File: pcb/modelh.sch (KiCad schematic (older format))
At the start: 43 parts, among them J1 USB_B, J2 Conn_01x16, J3 Conn_01x12, J4 Conn_01x04, J5 Conn_02x03_Odd_Even, J6 Conn_02x05_Odd_Even, SW1 SW_Push, U1 STM32F103C8Tx, U2 AMS1117-3.3, Y1 8MHz, Y2 32.768KHz

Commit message: WIP
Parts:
- removed D1: B5819W, Diode_SMD:D_SOD-123, symbol Device:D_Schottky
- added R?: 0, symbol Device:R
- R7, R8, R9: value 120 -> 60; footprint Resistor_SMD:R_0603_1608Metric -> Resistor_SMD:R_0805_2012Metric
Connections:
- net +5V: now also R?.1
- net D+: now also R11.1
- net D-: no longer R11.1
- net at J1.1 (VBUS): now also R?.2
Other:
- moved on the sheet: R11
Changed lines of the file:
@@
 P 8900 4600
 F 0 "R7" V 8850 4750 50  0000 C CNN
-F 1 "120" V 8900 4600 50  0000 C CNN
-F 2 "Resistor_SMD:R_0603_1608Metric" V 8830 4600 50  0001 C CNN
+F 1 "60" V 8900 4600 50  0000 C CNN
+F 2 "Resistor_SMD:R_0805_2012Metric" V 8830 4600 50  0001 C CNN
 F 3 "~" H 8900 4600 50  0001 C CNN
 F 4 "C22787" H 8900 4600 50  0001 C CNN "LCSC"
@@
 P 8900 4700
 F 0 "R8" V 8850 4850 50  0000 C CNN
-F 1 "120" V 8900 4700 50  0000 C CNN
-F 2 "Resistor_SMD:R_0603_1608Metric" V 8830 4700 50  0001 C CNN
+F 1 "60" V 8900 4700 50  0000 C CNN
+F 2 "Resistor_SMD:R_0805_2012Metric" V 8830 4700 50  0001 C CNN
 F 3 "~" H 8900 4700 50  0001 C CNN
 F 4 "C22787" H 8900 4700 50  0001 C CNN "LCSC"
@@
 P 8900 4900
 F 0 "R9" V 8850 5050 50  0000 C CNN
-F 1 "120" V 8900 4900 50  0000 C CNN
-F 2 "Resistor_SMD:R_0603_1608Metric" V 8830 4900 50  0001 C CNN
+F 1 "60" V 8900 4900 50  0000 C CNN
+F 2 "Resistor_SMD:R_0805_2012Metric" V 8830 4900 50  0001 C CNN
 F 3 "~" H 8900 4900 50  0001 C CNN
 F 4 "C22787" H 8900 4900 50  0001 C CNN "LCSC"
@@
 L power:+5V #PWR0104
 U 1 1 5EDAFF6A
-P 2250 1000
-F 0 "#PWR0104" H 2250 850 50  0001 C CNN
-F 1 "+5V" H 2265 1173 50  0000 C CNN
-F 2 "" H 2250 1000 50  0001 C CNN
-F 3 "" H 2250 1000 50  0001 C CNN
-	1    2250 1000
+P 2150 900
+F 0 "#PWR0104" H 2150 750 50  0001 C CNN
+F 1 "+5V" H 2165 1073 50  0000 C CNN
+F 2 "" H 2150 900 50  0001 C CNN
+F 3 "" H 2150 900 50  0001 C CNN
+	1    2150 900
 	1    0    0    -1
 $EndComp
 Wire Wire Line
 	1700 1100 1800 1100
-Wire Wire Line
-	2250 1100 2250 1000
 $Comp
 L Device:R R3
@@
 Wire Wire Line
 	1700 1400 1800 1400
-Wire Wire Line
-	2100 1400 2200 1400
 $Comp
 L Device:C C5
@@
 L Device:R R11
 U 1 1 5F3ACB58
-P 2200 1550
-F 0 "R11" H 2270 1596 50  0000 L CNN
-F 1 "1.5k" H 2270 1505 50  0000 L CNN
-F 2 "Resistor_SMD:R_0603_1608Metric" V 2130 1550 50  0001 C CNN
-F 3 "~" H 2200 1550 50  0001 C CNN
-	1    2200 1550
-	1    0    0    -1
-$EndComp
-Wire Wire Line
-	2350 1400 2200 1400
-Connection ~ 2200 1400
-Wire Wire Line
-	2100 1300 2350 1300
+P 2400 1100
+F 0 "R11" H 2470 1146 50  0000 L CNN
+F 1 "1.5k" H 2470 1055 50  0000 L CNN
+F 2 "Resistor_SMD:R_0603_1608Metric" V 2330 1100 50  0001 C CNN
+F 3 "~" H 2400 1100 50  0001 C CNN
+	1    2400 1100
+	-1   0    0    1
+$EndComp
 $Comp
 L power:+5V #PWR0124
 U 1 1 5F3CEBAA
-P 2200 1700
-F 0 "#PWR0124" H 2200 1550 50  0001 C CNN
-F 1 "+5V" H 2215 1873 50  0000 C CNN
-F 2 "" H 2200 1700 50  0001 C CNN
-F 3 "" H 2200 1700 50  0001 C CNN
-	1    2200 1700
-	-1   0    0    1
-$EndComp
-$Comp
-L Device:D_Schottky D1
-U 1 1 5F3E67EF
-P 1950 1100
-F 0 "D1" H 1950 884 50  0000 C CNN
-F 1 "B5819W" H 1950 975 50  0000 C CNN
-F 2 "Diode_SMD:D_SOD-123" H 1950 1100 50  0001 C CNN
-F 3 "~" H 1950 1100 50  0001 C CNN
-	1    1950 1100
-	-1   0    0    1
-$EndComp
-Wire Wire Line
-	2100 1100 2250 1100
+P 2400 950
+F 0 "#PWR0124" H 2400 800 50  0001 C CNN
+F 1 "+5V" H 2415 1123 50  0000 C CNN
+F 2 "" H 2400 950 50  0001 C CNN
+F 3 "" H 2400 950 50  0001 C CNN
+	1    2400 950
+	1    0    0    -1
+$EndComp
 Wire Wire Line
 	2900 5150 3200 5150
@@
 Text GLabel 8450 4900 0    50   Input ~ 0
 led2
-Text GLabel 2350 1300 2    50   Input ~ 0
+Text GLabel 2550 1300 2    50   Input ~ 0
 D+
-Text GLabel 2350 1400 2    50   Input ~ 0
+Text GLabel 2550 1400 2    50   Input ~ 0
 D-
 Text GLabel 1250 5150 0    50   Input ~ 0
@@
 Wire Wire Line
 	10100 4000 9900 4000
+Wire Wire Line
+	2400 1300 2400 1250
+Wire Wire Line
+	2100 1100 2150 1100
+Wire Wire Line
+	2150 1100 2150 900
+Wire Wire Line
+	2400 1300 2100 1300
+Wire Wire Line
+	2550 1300 2400 1300
+Connection ~ 2400 1300
+Wire Wire Line
+	2550 1400 2100 1400
+$Comp
+L Device:R R?
+U 1 1 5F9EF12F
+P 1950 1100
+F 0 "R?" V 1743 1100 50  0000 C CNN
+F 1 "0" V 1834 1100 50  0000 C CNN
+F 2 "" V 1880 1100 50  0001 C CNN
+F 3 "~" H 1950 1100 50  0001 C CNN
+	1    1950 1100
+	0    1    1    0
+$EndComp
 $EndSCHEMATC

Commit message: WIP
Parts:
- R16: renamed from R?; footprint (none) -> Resistor_SMD:R_0805_2012Metric_Pad1.15x1.40mm_HandSolder
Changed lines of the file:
@@
 	2550 1400 2100 1400
 $Comp
-L Device:R R?
+L Device:R R16
 U 1 1 5F9EF12F
 P 1950 1100
-F 0 "R?" V 1743 1100 50  0000 C CNN
+F 0 "R16" V 1743 1100 50  0000 C CNN
 F 1 "0" V 1834 1100 50  0000 C CNN
-F 2 "" V 1880 1100 50  0001 C CNN
+F 2 "Resistor_SMD:R_0805_2012Metric_Pad1.15x1.40mm_HandSolder" V 1880 1100 50  0001 C CNN
 F 3 "~" H 1950 1100 50  0001 C CNN
 	1    1950 1100

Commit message: WIP
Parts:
- J2: footprint Connector_PinHeader_2.54mm:PinHeader_1x16_P2.54mm_Vertical -> Connector_PinSocket_2.54mm:PinSocket_1x16_P2.54mm_Vertical
- J4: footprint Connector_PinHeader_2.54mm:PinHeader_1x04_P2.54mm_Vertical -> Connector_PinSocket_2.54mm:PinSocket_1x04_P2.54mm_Vertical
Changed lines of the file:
@@
 F 0 "J2" H 10380 1942 50  0000 L CNN
 F 1 "Conn_01x16" H 10380 1851 50  0000 L CNN
-F 2 "Connector_PinHeader_2.54mm:PinHeader_1x16_P2.54mm_Vertical" H 10300 1950 50  0001 C CNN
+F 2 "Connector_PinSocket_2.54mm:PinSocket_1x16_P2.54mm_Vertical" H 10300 1950 50  0001 C CNN
 F 3 "~" H 10300 1950 50  0001 C CNN
 	1    10300 1950
@@
 F 0 "J4" H 10380 4692 50  0000 L CNN
 F 1 "Conn_01x04" H 10380 4601 50  0000 L CNN
-F 2 "Connector_PinHeader_2.54mm:PinHeader_1x04_P2.54mm_Vertical" H 10300 4700 50  0001 C CNN
+F 2 "Connector_PinSocket_2.54mm:PinSocket_1x04_P2.54mm_Vertical" H 10300 4700 50  0001 C CNN
 F 3 "~" H 10300 4700 50  0001 C CNN
 	1    10300 4700

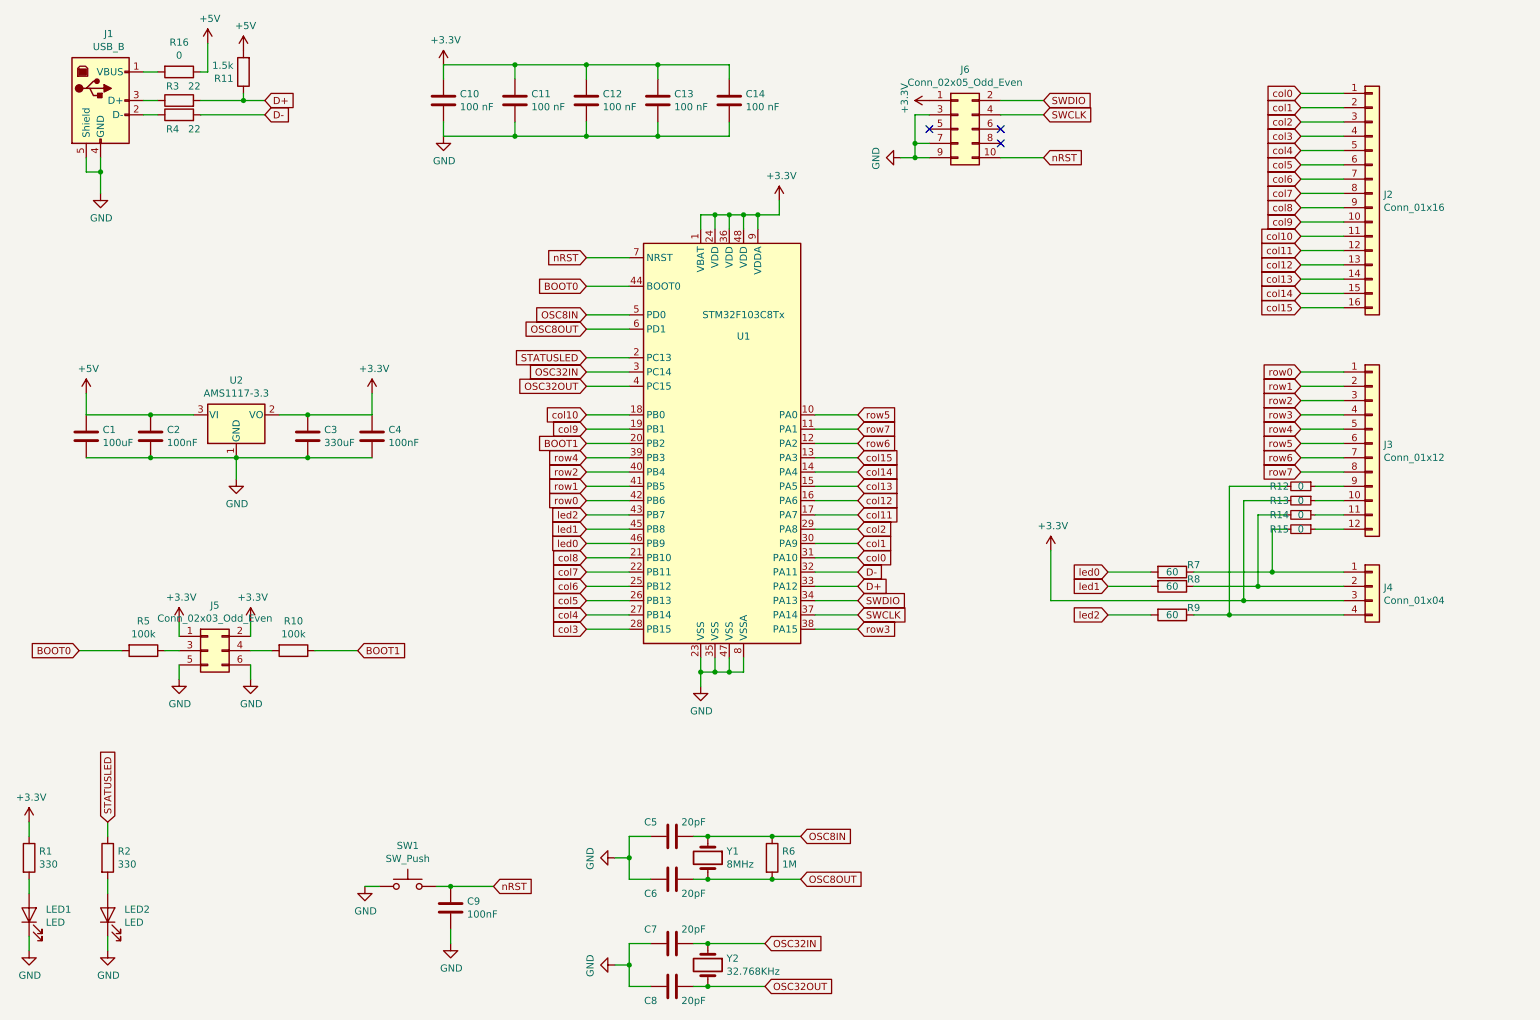
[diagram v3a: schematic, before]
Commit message: Remove LSE oscillator
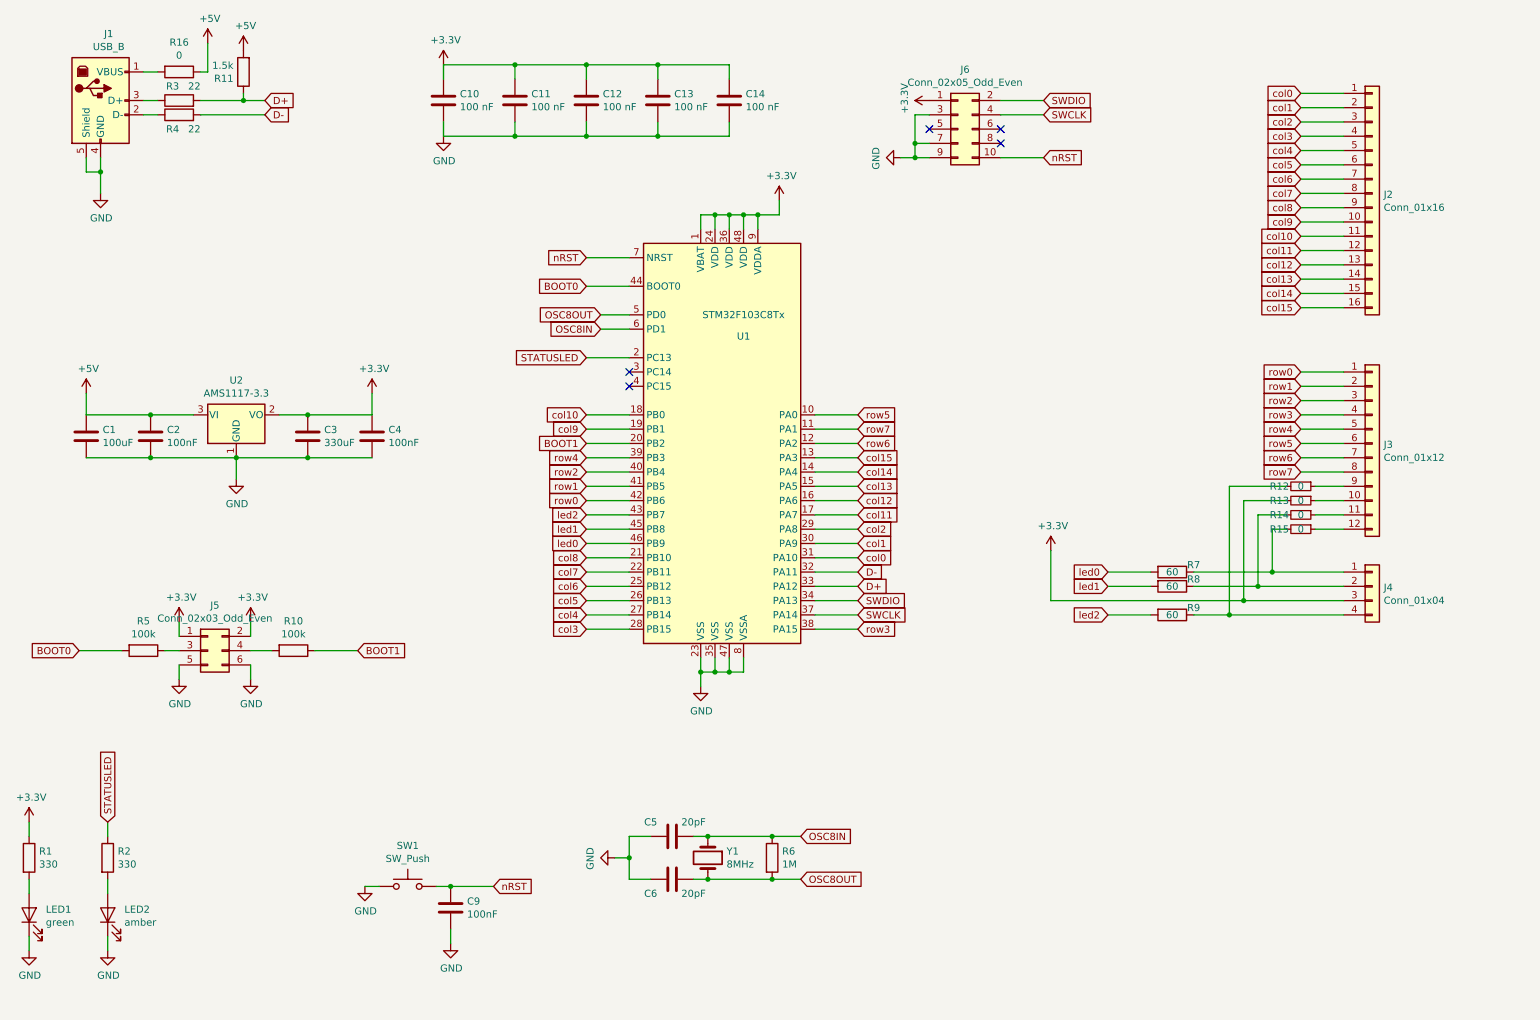
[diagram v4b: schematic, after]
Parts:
- removed C7, C8: 20pF, Capacitor_SMD:C_0603_1608Metric, symbol Device:C
- removed Y2: 32.768KHz, Crystal:Crystal_SMD_3215-2Pin_3.2x1.5mm, symbol Device:Crystal
- LED1: value LED -> green
- LED2: value LED -> amber
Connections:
- net OSC8IN: now also U1.6 (PD1); no longer U1.5 (PD0)
- net OSC8OUT: now also U1.5 (PD0); no longer U1.6 (PD1)
- net OSC32IN: no longer names the net of U1.3 (PC14)
- net OSC32OUT: no longer names the net of U1.4 (PC15)
- no-connect marks 3 -> 5
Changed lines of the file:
@@
 P 900 7000
 F 0 "LED1" V 939 6883 50  0000 R CNN
-F 1 "LED" V 848 6883 50  0000 R CNN
+F 1 "green" V 848 6883 50  0000 R CNN
 F 2 "LED_SMD:LED_0805_2012Metric" H 900 7000 50  0001 C CNN
 F 3 "~" H 900 7000 50  0001 C CNN
@@
 	5100 4100 4800 4100
 Wire Wire Line
-	5100 2800 4800 2800
-Wire Wire Line
-	4800 2900 5100 2900
-Wire Wire Line
-	5100 3200 4800 3200
-Wire Wire Line
-	4800 3300 5100 3300
-Wire Wire Line
 	5100 2400 4800 2400
 Wire Wire Line
@@
 Wire Wire Line
 	5550 6750 5650 6750
-$Comp
-L Device:C C7
-U 1 1 5F13915E
-P 5400 7200
-F 0 "C7" V 5300 7050 50  0000 C CNN
-F 1 "20pF" V 5300 7350 50  0000 C CNN
-F 2 "Capacitor_SMD:C_0603_1608Metric" H 5438 7050 50  0001 C CNN
-F 3 "~" H 5400 7200 50  0001 C CNN
-F 4 "C1653" H 5400 7200 50  0001 C CNN "LCSC"
-	1    5400 7200
-	0    1    1    0
-$EndComp
-$Comp
-L Device:C C8
-U 1 1 5F139165
-P 5400 7500
-F 0 "C8" V 5500 7350 50  0000 C CNN
-F 1 "20pF" V 5500 7650 50  0000 C CNN
-F 2 "Capacitor_SMD:C_0603_1608Metric" H 5438 7350 50  0001 C CNN
-F 3 "~" H 5400 7500 50  0001 C CNN
-F 4 "C1653" H 5400 7500 50  0001 C CNN "LCSC"
-	1    5400 7500
-	0    1    1    0
-$EndComp
-Wire Wire Line
-	5250 7200 5100 7200
-Wire Wire Line
-	5100 7500 5250 7500
-Wire Wire Line
-	5100 7200 5100 7350
-$Comp
-L power:GND #PWR0106
-U 1 1 5F13916E
-P 5000 7350
-F 0 "#PWR0106" H 5000 7100 50  0001 C CNN
-F 1 "GND" H 5005 7177 50  0000 C CNN
-F 2 "" H 5000 7350 50  0001 C CNN
-F 3 "" H 5000 7350 50  0001 C CNN
-	1    5000 7350
-	0    1    1    0
-$EndComp
-Connection ~ 5100 7350
-Wire Wire Line
-	5100 7350 5100 7500
-Wire Wire Line
-	5000 7350 5100 7350
-$Comp
-L Device:Crystal Y2
-U 1 1 5F139177
-P 5650 7350
-F 0 "Y2" V 5604 7481 50  0000 L CNN
-F 1 "32.768KHz" V 5695 7481 50  0000 L CNN
-F 2 "Crystal:Crystal_SMD_3215-2Pin_3.2x1.5mm" H 5650 7350 50  0001 C CNN
-F 3 "~" H 5650 7350 50  0001 C CNN
-	1    5650 7350
-	0    1    1    0
-$EndComp
-Wire Wire Line
-	5550 7200 5650 7200
-Connection ~ 5650 7200
-Wire Wire Line
-	5550 7500 5650 7500
-Connection ~ 5650 7500
 $Comp
 L Device:R R6
@@
 Connection ~ 5650 6750
 Wire Wire Line
-	5650 7200 6050 7200
-Wire Wire Line
-	5650 7500 6050 7500
-Wire Wire Line
 	6300 6750 6100 6750
 Connection ~ 6100 6750
@@
 P 1450 7000
 F 0 "LED2" V 1489 6883 50  0000 R CNN
-F 1 "LED" V 1398 6883 50  0000 R CNN
+F 1 "amber" V 1398 6883 50  0000 R CNN
 F 2 "LED_SMD:LED_0805_2012Metric" H 1450 7000 50  0001 C CNN
 F 3 "~" H 1450 7000 50  0001 C CNN
@@
 Text GLabel 4150 6800 2    50   Input ~ 0
 nRST
-Text GLabel 6050 7500 2    50   Input ~ 0
-OSC32OUT
-Text GLabel 6050 7200 2    50   Input ~ 0
-OSC32IN
 Text GLabel 6300 6750 2    50   Input ~ 0
 OSC8OUT
@@
 Text GLabel 4800 2600 0    50   Input ~ 0
 BOOT0
-Text GLabel 4800 2800 0    50   Input ~ 0
-OSC8IN
-Text GLabel 4800 2900 0    50   Input ~ 0
-OSC8OUT
 Text GLabel 4800 3100 0    50   Input ~ 0
 STATUSLED
-Text GLabel 4800 3200 0    50   Input ~ 0
-OSC32IN
-Text GLabel 4800 3300 0    50   Input ~ 0
-OSC32OUT
 Text GLabel 4800 3500 0    50   Input ~ 0
 col10
@@
 	0    1    1    0
 $EndComp
+Wire Wire Line
+	4900 2800 5100 2800
+Wire Wire Line
+	4900 2900 5100 2900
+Text GLabel 4900 2800 0    50   Input ~ 0
+OSC8OUT
+Text GLabel 4900 2900 0    50   Input ~ 0
+OSC8IN
+NoConn ~ 5100 3200
+NoConn ~ 5100 3300
 $EndSCHEMATC

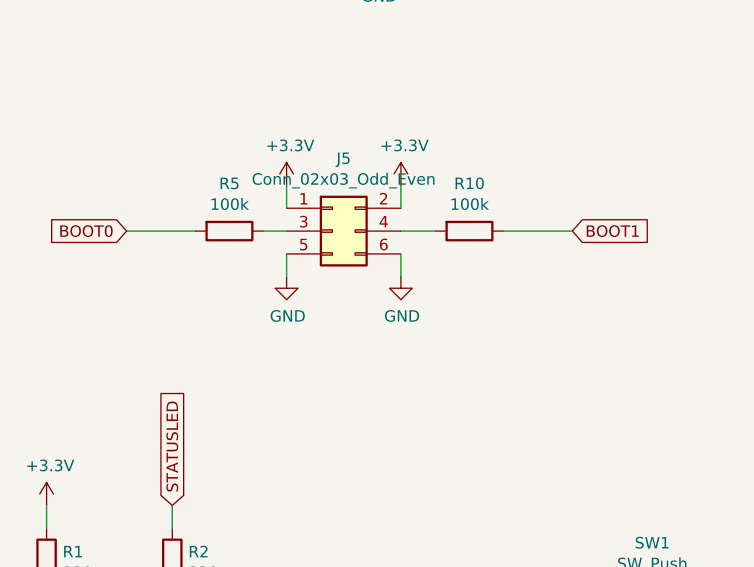
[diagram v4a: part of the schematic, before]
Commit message: Make boot selection pins optional
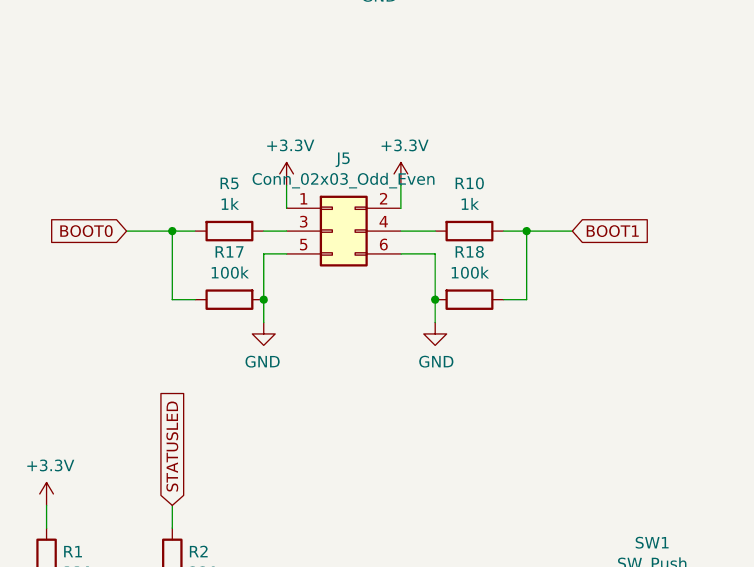
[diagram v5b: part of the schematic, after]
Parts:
- added R17, R18: 100k, Resistor_SMD:R_0603_1608Metric, symbol Device:R
- R10, R5: value 100k -> 1k
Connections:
- net BOOT0: now also R17.1
- net BOOT1: now also R18.1
- net GND: now also R17.2, R18.2
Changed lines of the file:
@@
 P 2750 5150
 F 0 "R10" V 2543 5150 50  0000 C CNN
-F 1 "100k" V 2634 5150 50  0000 C CNN
+F 1 "1k" V 2634 5150 50  0000 C CNN
 F 2 "Resistor_SMD:R_0603_1608Metric" V 2680 5150 50  0001 C CNN
 F 3 "~" H 2750 5150 50  0001 C CNN
@@
 P 1700 5150
 F 0 "R5" V 1493 5150 50  0000 C CNN
-F 1 "100k" V 1584 5150 50  0000 C CNN
+F 1 "1k" V 1584 5150 50  0000 C CNN
 F 2 "Resistor_SMD:R_0603_1608Metric" V 1630 5150 50  0001 C CNN
 F 3 "~" H 1700 5150 50  0001 C CNN
@@
 	1950 5150 1850 5150
 Wire Wire Line
-	1550 5150 1250 5150
+	1550 5150 1450 5150
 $Comp
 L power:+3.3V #PWR0116
@@
 L power:GND #PWR0118
 U 1 1 5F4D0580
-P 2450 5350
-F 0 "#PWR0118" H 2450 5100 50  0001 C CNN
-F 1 "GND" H 2455 5177 50  0000 C CNN
-F 2 "" H 2450 5350 50  0001 C CNN
-F 3 "" H 2450 5350 50  0001 C CNN
-	1    2450 5350
-	1    0    0    -1
-$EndComp
-Wire Wire Line
-	2450 5350 2450 5250
-$Comp
-L power:GND #PWR0119
-U 1 1 5F4D8778
-P 1950 5350
-F 0 "#PWR0119" H 1950 5100 50  0001 C CNN
-F 1 "GND" H 1955 5177 50  0000 C CNN
-F 2 "" H 1950 5350 50  0001 C CNN
-F 3 "" H 1950 5350 50  0001 C CNN
-	1    1950 5350
-	1    0    0    -1
-$EndComp
-Wire Wire Line
-	1950 5350 1950 5250
+P 2600 5550
+F 0 "#PWR0118" H 2600 5300 50  0001 C CNN
+F 1 "GND" H 2605 5377 50  0000 C CNN
+F 2 "" H 2600 5550 50  0001 C CNN
+F 3 "" H 2600 5550 50  0001 C CNN
+	1    2600 5550
+	1    0    0    -1
+$EndComp
+Wire Wire Line
+	2600 5550 2600 5450
 Wire Wire Line
 	2450 5050 2450 4950
@@
 $EndComp
 Wire Wire Line
-	2900 5150 3200 5150
+	2900 5150 3000 5150
 Wire Wire Line
 	5100 3700 4800 3700
@@
 NoConn ~ 5100 3200
 NoConn ~ 5100 3300
+$Comp
+L Device:R R18
+U 1 1 5F1AC946
+P 2750 5450
+F 0 "R18" V 2543 5450 50  0000 C CNN
+F 1 "100k" V 2634 5450 50  0000 C CNN
+F 2 "Resistor_SMD:R_0603_1608Metric" V 2680 5450 50  0001 C CNN
+F 3 "~" H 2750 5450 50  0001 C CNN
+	1    2750 5450
+	0    1    1    0
+$EndComp
+Wire Wire Line
+	2900 5450 3000 5450
+Wire Wire Line
+	3000 5450 3000 5150
+Connection ~ 3000 5150
+Wire Wire Line
+	3000 5150 3200 5150
+$Comp
+L power:GND #PWR0106
+U 1 1 5F1D1EEB
+P 1850 5550
+F 0 "#PWR0106" H 1850 5300 50  0001 C CNN
+F 1 "GND" H 1855 5377 50  0000 C CNN
+F 2 "" H 1850 5550 50  0001 C CNN
+F 3 "" H 1850 5550 50  0001 C CNN
+	1    1850 5550
+	-1   0    0    -1
+$EndComp
+Wire Wire Line
+	1850 5550 1850 5450
+$Comp
+L Device:R R17
+U 1 1 5F1D1EF2
+P 1700 5450
+F 0 "R17" V 1493 5450 50  0000 C CNN
+F 1 "100k" V 1584 5450 50  0000 C CNN
+F 2 "Resistor_SMD:R_0603_1608Metric" V 1630 5450 50  0001 C CNN
+F 3 "~" H 1700 5450 50  0001 C CNN
+	1    1700 5450
+	0    -1   1    0
+$EndComp
+Wire Wire Line
+	1550 5450 1450 5450
+Wire Wire Line
+	2450 5250 2600 5250
+Wire Wire Line
+	2600 5250 2600 5450
+Connection ~ 2600 5450
+Wire Wire Line
+	1850 5450 1850 5250
+Wire Wire Line
+	1850 5250 1950 5250
+Connection ~ 1850 5450
+Wire Wire Line
+	1450 5450 1450 5150
+Connection ~ 1450 5150
+Wire Wire Line
+	1450 5150 1250 5150
 $EndSCHEMATC
